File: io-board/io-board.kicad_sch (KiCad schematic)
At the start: 9 parts, among them J1 Conn_01x03, J2 Conn_01x03, J3 Conn_01x03, J4 Conn_01x03, J5 Conn_01x24

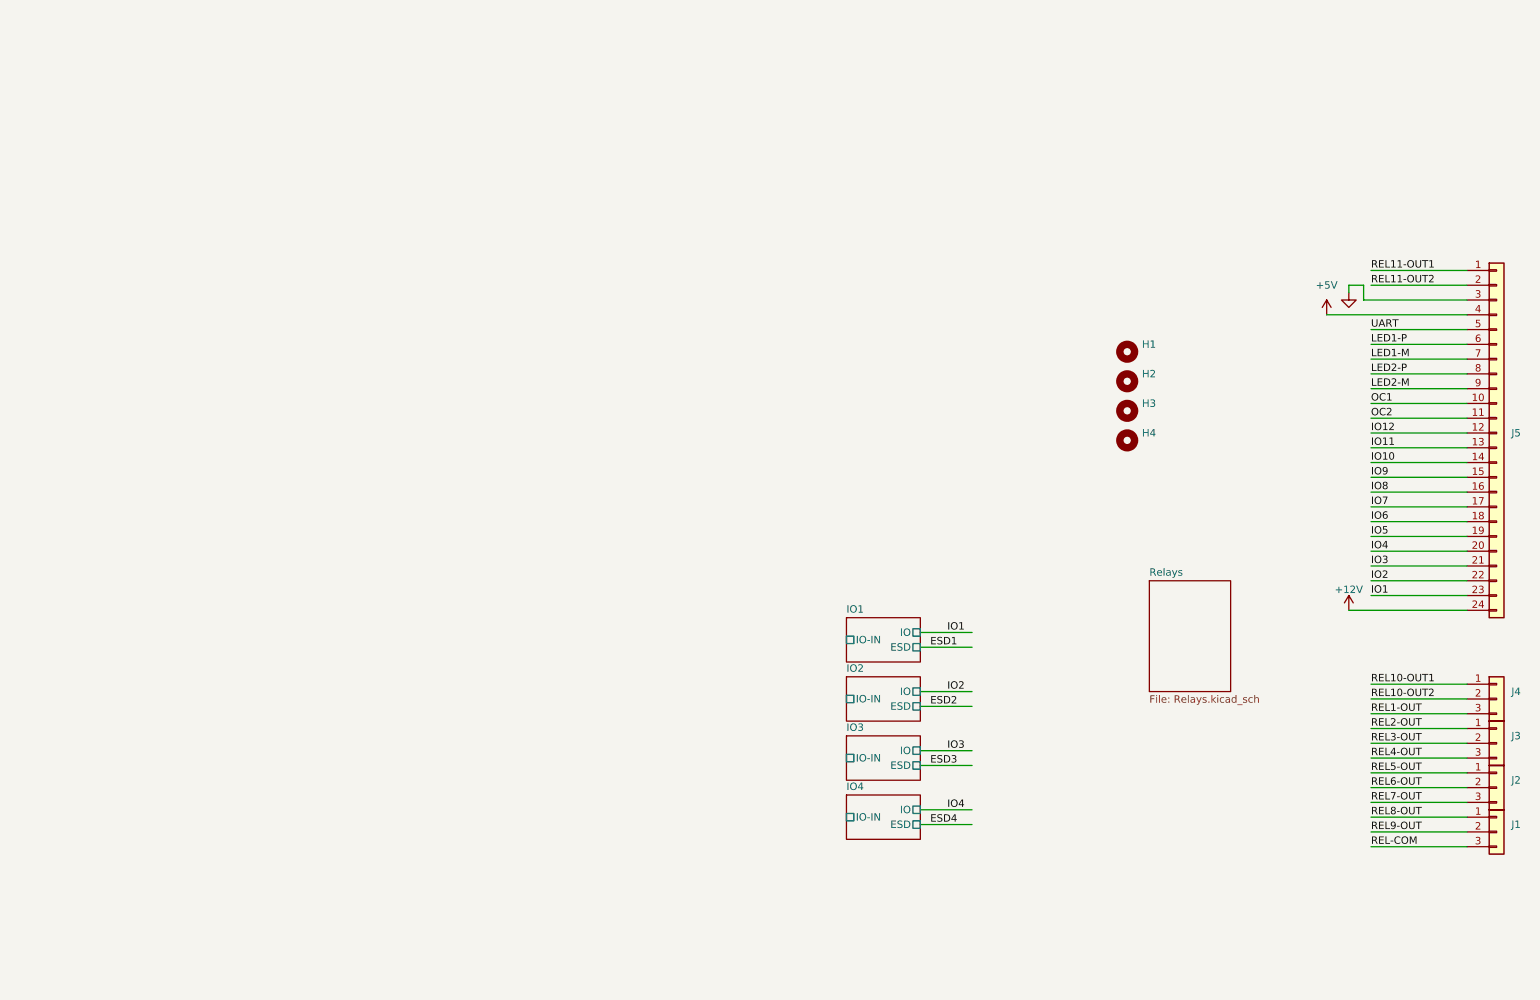
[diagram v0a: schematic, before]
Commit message: Add STM32 module
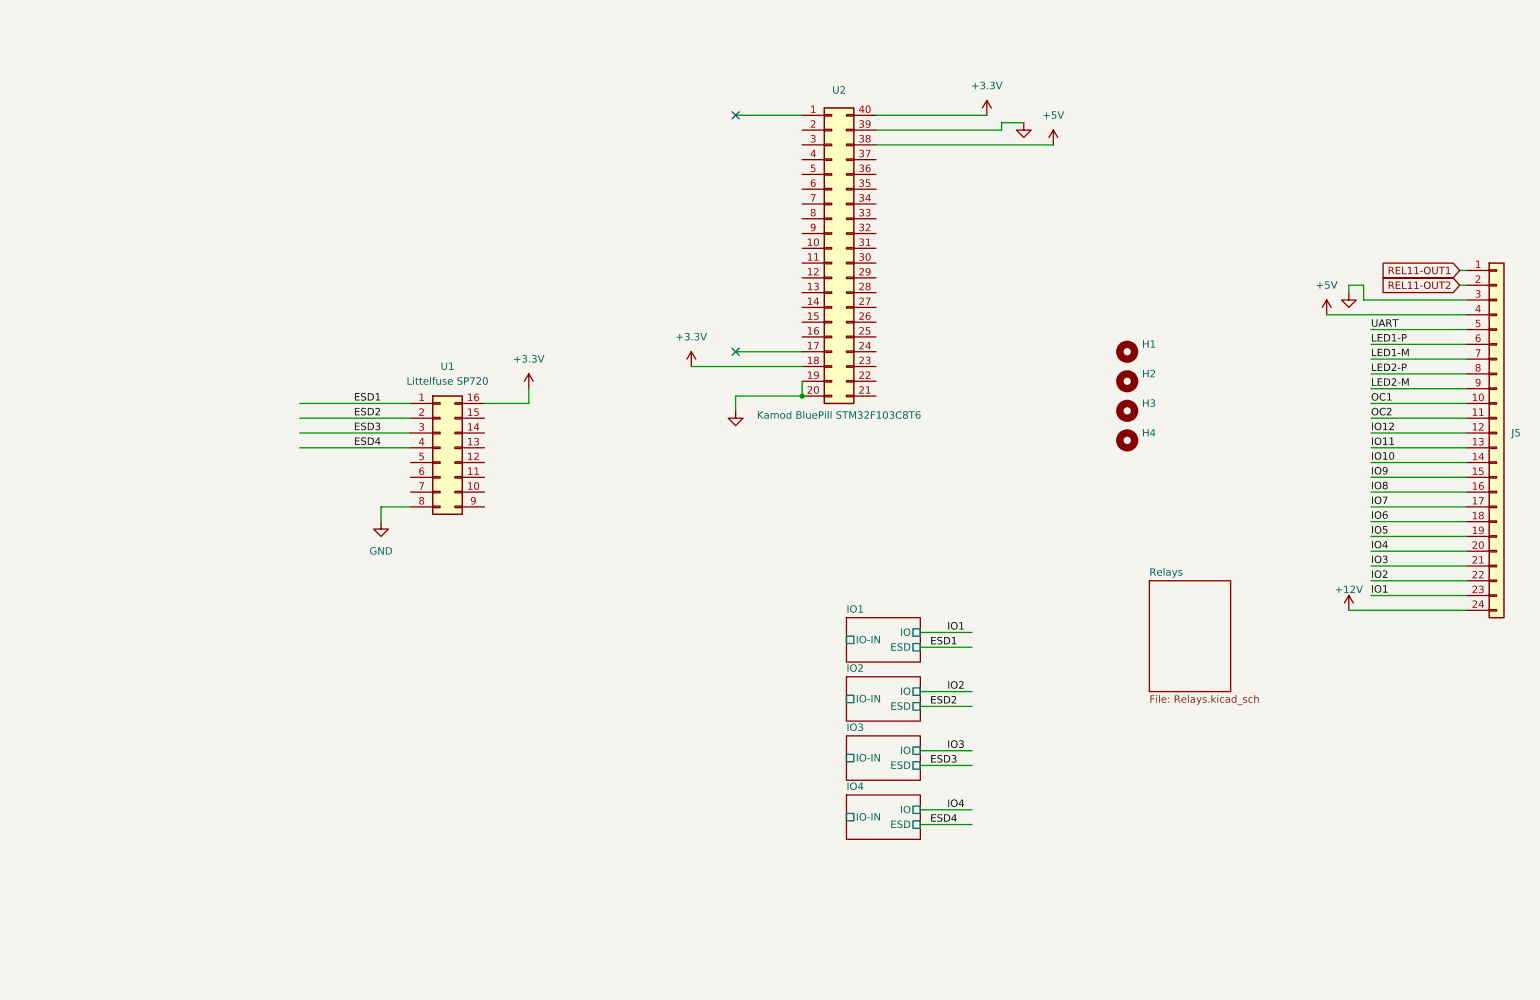
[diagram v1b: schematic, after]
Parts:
- removed J1, J2, J3, J4: Conn_01x03, Footprints:DG128-5.0-03P-14-00A-H, symbol Connector_Generic:Conn_01x03
- added U1: Littelfuse SP720, Package_SO:SOIC-16_4.55x10.3mm_P1.27mm, symbol Connector_Generic:Conn_02x08_Counter_Clockwise
- added U2: Kamod BluePill STM32F103C8T6, Footprints:Kamod-BluePill-STM32F103C8T6, symbol Connector_Generic:Conn_02x20_Counter_Clockwise
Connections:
- net +5V: now also U2.38 (Pin_38)
- net ESD1: now also U1.1 (Pin_1)
- net ESD2: now also U1.2 (Pin_2)
- net ESD3: now also U1.3 (Pin_3)
- net ESD4: now also U1.4 (Pin_4)
- net GND: now also U1.8 (Pin_8), U2.19 (Pin_19), U2.20 (Pin_20), U2.39 (Pin_39)
- new net +3.3V: U1.16 (Pin_16), U2.18 (Pin_18), U2.40 (Pin_40)
- no-connect marks 0 -> 2

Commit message: Almost all connected except OC and LED drivers
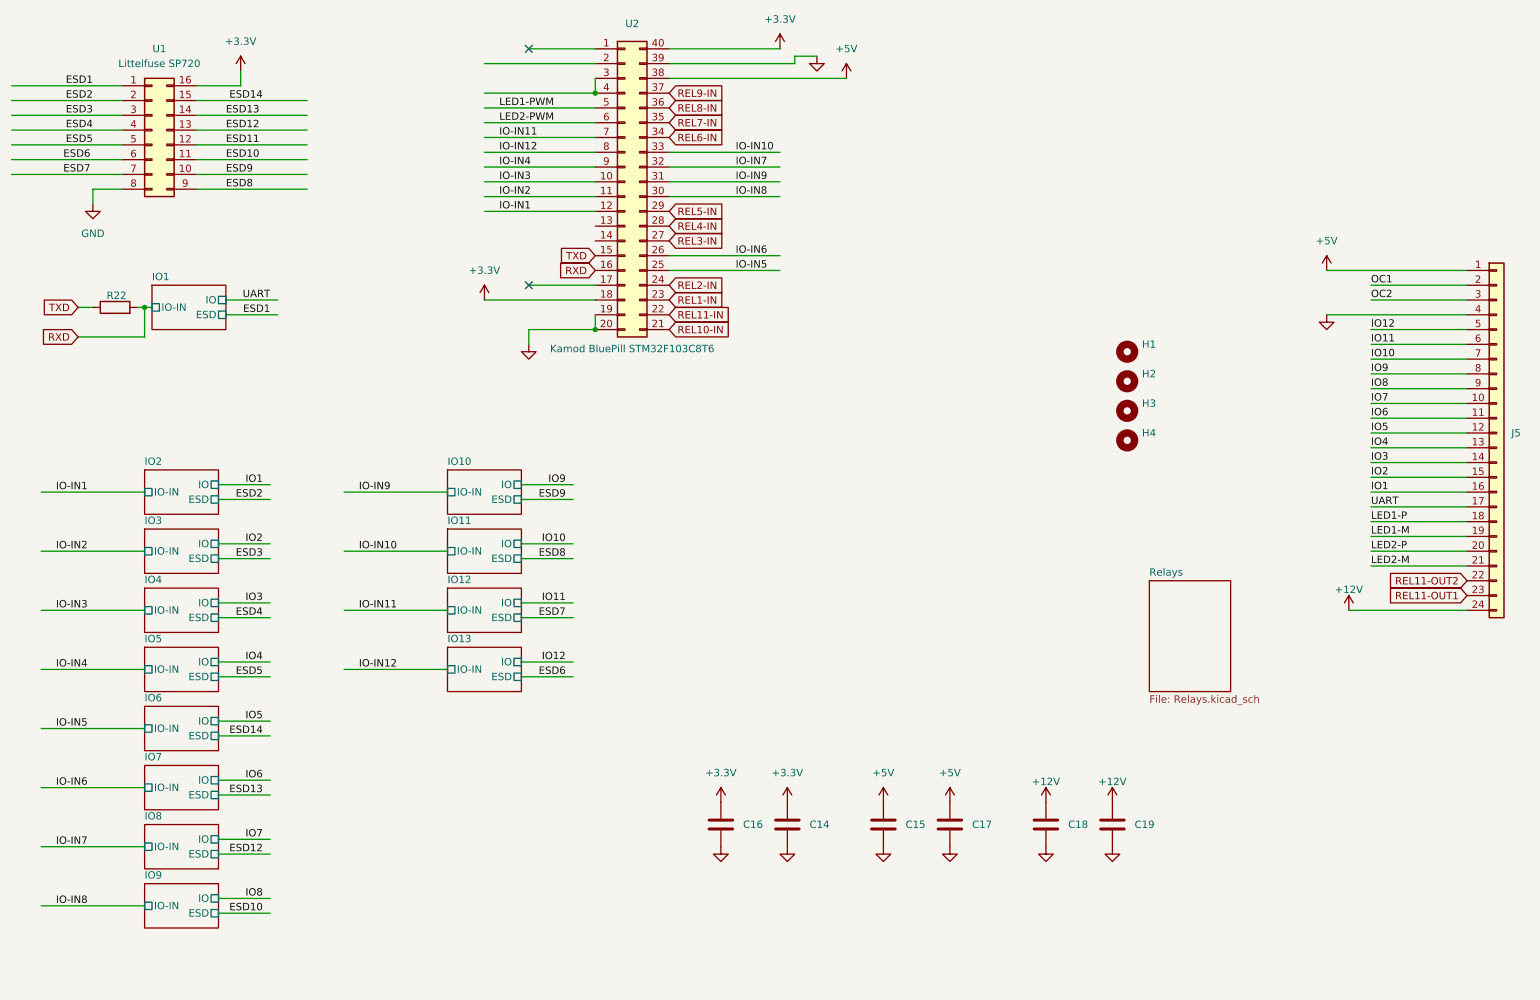
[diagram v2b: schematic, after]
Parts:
- added C14, C15, C16, C17, C18, C19: C, Capacitor_SMD:C_0805_2012Metric_Pad1.18x1.45mm_HandSolder, symbol Device:C
- added R22: R, Resistor_SMD:R_0805_2012Metric_Pad1.20x1.40mm_HandSolder, symbol Device:R
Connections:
- net +12V: now also C18.1, C19.1
- net +3.3V: now also C14.1, C16.1
- net +5V: now also J5.1 (Pin_1), C15.1, C17.1; no longer J5.4 (Pin_4)
- net GND: now also J5.4 (Pin_4), C14.2, C15.2, C16.2, C17.2, C18.2, C19.2; no longer J5.3 (Pin_3)
- net IO1: now also J5.16 (Pin_16); no longer J5.23 (Pin_23)
- net IO10: now also J5.7 (Pin_7); no longer J5.14 (Pin_14)
- net IO11: now also J5.6 (Pin_6); no longer J5.13 (Pin_13)
- net IO12: now also J5.5 (Pin_5); no longer J5.12 (Pin_12)
- net IO2: now also J5.15 (Pin_15); no longer J5.22 (Pin_22)
- net IO3: now also J5.14 (Pin_14); no longer J5.21 (Pin_21)
- net IO4: now also J5.13 (Pin_13); no longer J5.20 (Pin_20)
- net IO5: now also J5.12 (Pin_12); no longer J5.19 (Pin_19)
- net IO6: now also J5.11 (Pin_11); no longer J5.18 (Pin_18)
- net IO7: now also J5.10 (Pin_10); no longer J5.17 (Pin_17)
- net IO8: now also J5.9 (Pin_9); no longer J5.16 (Pin_16)
- net IO9: now also J5.8 (Pin_8); no longer J5.15 (Pin_15)
- net LED1-M: now also J5.19 (Pin_19); no longer J5.7 (Pin_7)
- net LED1-P: now also J5.18 (Pin_18); no longer J5.6 (Pin_6)
- net LED2-M: now also J5.21 (Pin_21); no longer J5.9 (Pin_9)
- net LED2-P: now also J5.20 (Pin_20); no longer J5.8 (Pin_8)
- net OC1: now also J5.2 (Pin_2); no longer J5.10 (Pin_10)
- net OC2: now also J5.3 (Pin_3); no longer J5.11 (Pin_11)
- net REL11-OUT1: now also J5.23 (Pin_23); no longer J5.1 (Pin_1)
- net REL11-OUT2: now also J5.22 (Pin_22); no longer J5.2 (Pin_2)
- net UART: now also J5.17 (Pin_17); no longer J5.5 (Pin_5)
- net ESD9: now reaches U1.10 (Pin_10)
- net ESD10: now reaches U1.11 (Pin_11)
- net ESD11: now reaches U1.12 (Pin_12)
- net ESD12: now reaches U1.13 (Pin_13)
- net ESD13: now reaches U1.14 (Pin_14)
- net ESD14: now reaches U1.15 (Pin_15)
- net ESD5: now reaches U1.5 (Pin_5)
- net ESD6: now reaches U1.6 (Pin_6)
- net ESD7: now reaches U1.7 (Pin_7)
- net ESD8: now reaches U1.9 (Pin_9)
- net IO-IN3: now reaches U2.10 (Pin_10)
- net IO-IN2: now reaches U2.11 (Pin_11)
- net IO-IN1: now reaches U2.12 (Pin_12)
- net TXD: now reaches U2.15 (Pin_15)
- net TXD: now also R22.1
- net RXD: now reaches U2.16 (Pin_16)
- net RXD: now also R22.2
- net REL10-IN: now reaches U2.21 (Pin_21)
- net REL11-IN: now reaches U2.22 (Pin_22)
- net REL1-IN: now reaches U2.23 (Pin_23)
- net REL2-IN: now reaches U2.24 (Pin_24)
- net IO-IN5: now reaches U2.25 (Pin_25)
- net IO-IN6: now reaches U2.26 (Pin_26)
- net REL3-IN: now reaches U2.27 (Pin_27)
- net REL4-IN: now reaches U2.28 (Pin_28)
- net REL5-IN: now reaches U2.29 (Pin_29)
- net at U2.3 (Pin_3): now also U2.4 (Pin_4)
- net IO-IN8: now reaches U2.30 (Pin_30)
- net IO-IN9: now reaches U2.31 (Pin_31)
- net IO-IN7: now reaches U2.32 (Pin_32)
- net IO-IN10: now reaches U2.33 (Pin_33)
- net REL6-IN: now reaches U2.34 (Pin_34)
- net REL7-IN: now reaches U2.35 (Pin_35)
- net REL8-IN: now reaches U2.36 (Pin_36)
- net REL9-IN: now reaches U2.37 (Pin_37)
- net LED1-PWM: now reaches U2.5 (Pin_5)
- net LED2-PWM: now reaches U2.6 (Pin_6)
- net IO-IN11: now reaches U2.7 (Pin_7)
- net IO-IN12: now reaches U2.8 (Pin_8)
- net IO-IN4: now reaches U2.9 (Pin_9)
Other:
- added sheet IO10 (IO.kicad_sch)
- added sheet IO11 (IO.kicad_sch)
- added sheet IO12 (IO.kicad_sch)
- added sheet IO13 (IO.kicad_sch)
- added sheet IO5 (IO.kicad_sch)
- added sheet IO6 (IO.kicad_sch)
- added sheet IO7 (IO.kicad_sch)
- added sheet IO8 (IO.kicad_sch)
- added sheet IO9 (IO.kicad_sch)
- moved on the sheet: U1, U2

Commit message: All added and connected in PCB. Cleanup needed.
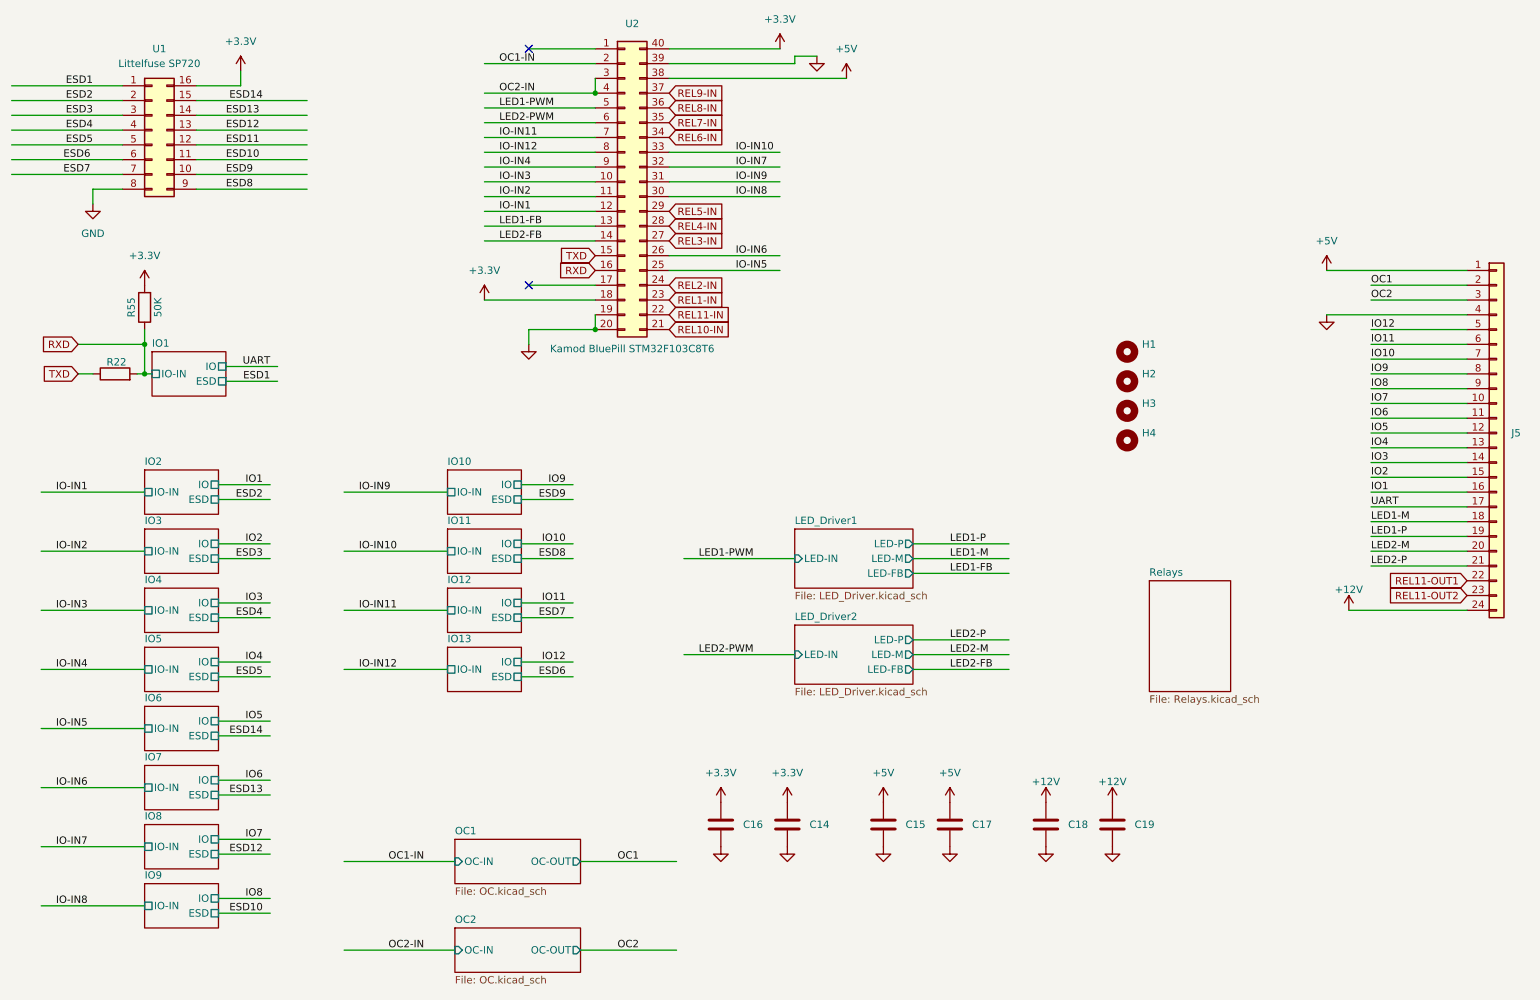
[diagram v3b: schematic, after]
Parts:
- added R55: 50K, Resistor_SMD:R_0805_2012Metric_Pad1.20x1.40mm_HandSolder, symbol Device:R
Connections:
- net +3.3V: now also R55.2
- net LED1-M: now also J5.18 (Pin_18); no longer J5.19 (Pin_19)
- net LED1-P: now also J5.19 (Pin_19); no longer J5.18 (Pin_18)
- net LED2-M: now also J5.20 (Pin_20); no longer J5.21 (Pin_21)
- net LED2-P: now also J5.21 (Pin_21); no longer J5.20 (Pin_20)
- net REL11-OUT1: now also J5.22 (Pin_22); no longer J5.23 (Pin_23)
- net REL11-OUT2: now also J5.23 (Pin_23); no longer J5.22 (Pin_22)
- net RXD: now also R55.1
- net LED1-FB: now reaches U2.13 (Pin_13)
- net LED2-FB: now reaches U2.14 (Pin_14)
- net OC1-IN: now reaches U2.2 (Pin_2)
- net OC2-IN: now reaches U2.3 (Pin_3), U2.4 (Pin_4)
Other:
- added sheet LED_Driver1 (LED_Driver.kicad_sch)
- added sheet LED_Driver2 (LED_Driver.kicad_sch)
- added sheet OC1 (OC.kicad_sch)
- added sheet OC2 (OC.kicad_sch)
- moved on the sheet: R22
